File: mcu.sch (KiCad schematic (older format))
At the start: 6 parts

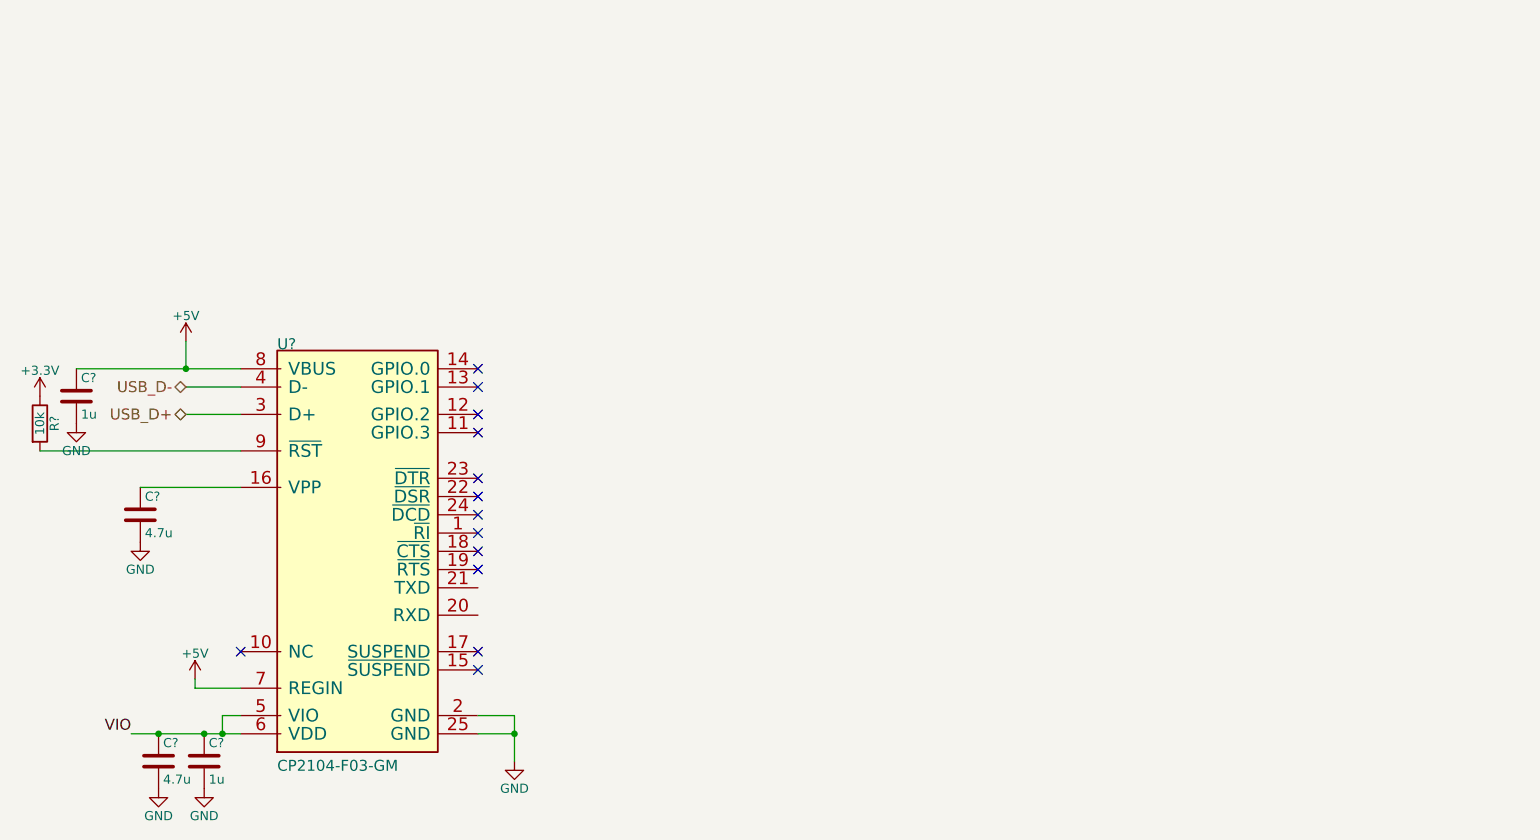
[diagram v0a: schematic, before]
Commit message: Finish basic MCU + USB/UART bridge schematics.
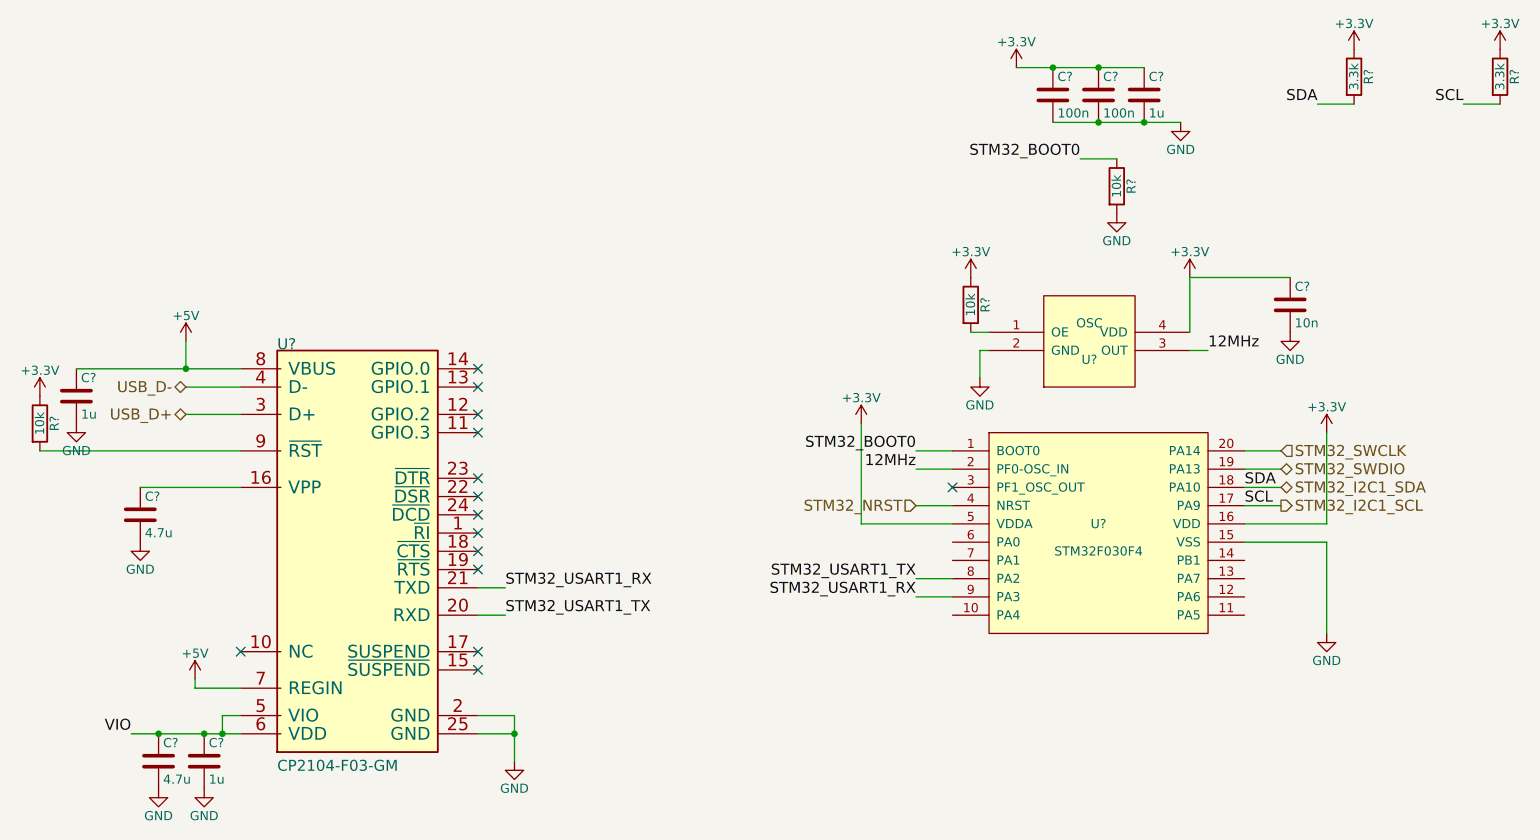
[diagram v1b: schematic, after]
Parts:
- added C?: 10n, symbol C
- added C? (x2): 100n, symbol C
- added C?: 1u, symbol C
- added R? (x2): 10k, symbol R
- added R? (x2): 3.3k, symbol R
- added U?: STM32F030F4, symbol STM32F030F4
- added U?: OSC, MODULE, symbol OSC
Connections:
- net +3V3: now also C?.1, C?.1, C?.1, C?.1, R?.1, R?.1, R?.1, U?.16 (VDD), U?.4 (VDD), U?.5 (VDDA)
- net GND: now also C?.2, C?.2, C?.2, C?.2, R?.2, U?.15 (VSS), U?.2 (GND)
- net STM32_USART1_TX: now reaches U?.20 (RXD)
- net STM32_USART1_TX: now also U?.8 (PA2)
- net STM32_USART1_RX: now reaches U?.21 (TXD)
- net STM32_USART1_RX: now also U?.9 (PA3)
- new net: R?.2, U?.1 (OE)
- new net 12MHz: U?.2 (PF0-OSC_IN), U?.3 (OUT)
- new net STM32_BOOT0: R?.1, U?.1 (BOOT0)
- new net STM32_I2C1_SCL: R?.2, U?.17 (PA9)
- new net STM32_I2C1_SDA: R?.2, U?.18 (PA10)
- new net STM32_NRST: U?.4 (NRST)
- new net STM32_SWCLK: U?.20 (PA14)
- new net STM32_SWDIO: U?.19 (PA13)
- no-connect marks 13 -> 14

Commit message: Add the config resistor dividers to the LTC3883 and output connectors, and a handful of test points. Schematic probably almost done at this point.
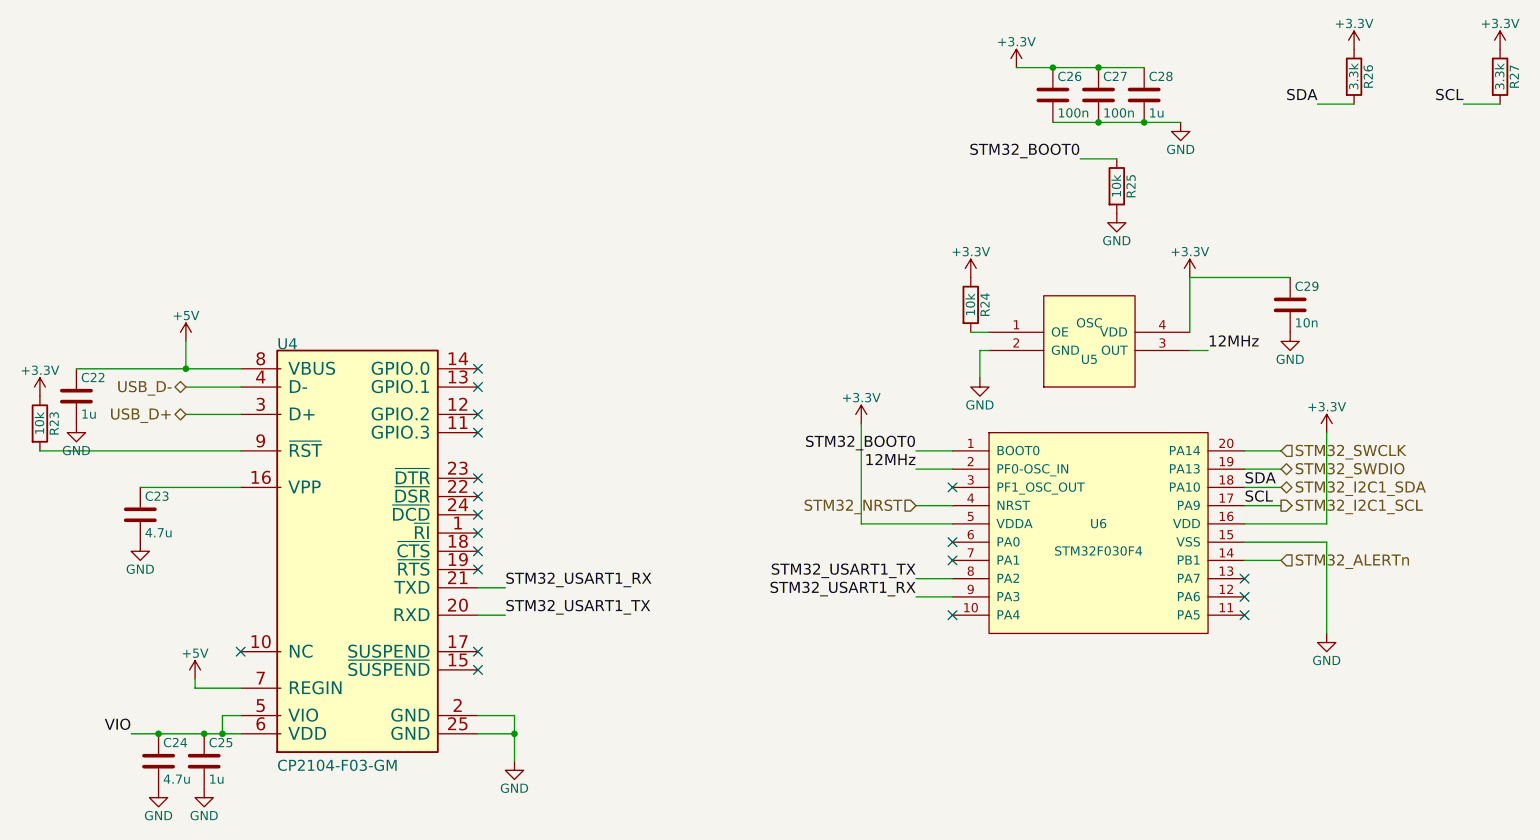
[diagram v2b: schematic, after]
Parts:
- gave numbers to parts that had none: 16
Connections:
- net STM32_ALERTn: now reaches U6.14 (PB1)
- no-connect marks 14 -> 20
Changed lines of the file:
@@
 $EndDescr
 $Comp
-L CP2104-F03-GM U?
+L CP2104-F03-GM U4
 U 1 1 569E6C41
 P 3550 2450
-F 0 "U?" H 3550 2450 60  0000 L BNN
+F 0 "U4" H 3550 2450 60  0000 L BNN
 F 1 "CP2104-F03-GM" H 3550 140 60  0000 L BNN
 F 2 "" H 3550 2450 60  0000 C CNN
@@
 $EndComp
 $Comp
-L +5V #PWR?
+L +5V #PWR41
 U 1 1 569E6CCC
 P 3050 2400
-F 0 "#PWR?" H 3050 2250 50  0001 C CNN
+F 0 "#PWR41" H 3050 2250 50  0001 C CNN
 F 1 "+5V" H 3050 2540 50  0000 C CNN
 F 2 "" H 3050 2400 50  0000 C CNN
@@
 $EndComp
 $Comp
-L C C?
+L C C22
 U 1 1 569E6CE5
 P 2450 2700
-F 0 "C?" H 2475 2800 50  0000 L CNN
+F 0 "C22" H 2475 2800 50  0000 L CNN
 F 1 "1u" H 2475 2600 50  0000 L CNN
 F 2 "" H 2488 2550 50  0000 C CNN
@@
 $EndComp
 $Comp
-L GND #PWR?
+L GND #PWR38
 U 1 1 569E6D2B
 P 2450 2850
-F 0 "#PWR?" H 2450 2600 50  0001 C CNN
+F 0 "#PWR38" H 2450 2600 50  0001 C CNN
 F 1 "GND" H 2450 2700 50  0000 C CNN
 F 2 "" H 2450 2850 50  0000 C CNN
@@
 $EndComp
 $Comp
-L C C?
+L C C23
 U 1 1 569E6D69
 P 2800 3350
-F 0 "C?" H 2825 3450 50  0000 L CNN
+F 0 "C23" H 2825 3450 50  0000 L CNN
 F 1 "4.7u" H 2825 3250 50  0000 L CNN
 F 2 "" H 2838 3200 50  0000 C CNN
@@
 $EndComp
 $Comp
-L GND #PWR?
+L GND #PWR39
 U 1 1 569E6DB5
 P 2800 3500
-F 0 "#PWR?" H 2800 3250 50  0001 C CNN
+F 0 "#PWR39" H 2800 3250 50  0001 C CNN
 F 1 "GND" H 2800 3350 50  0000 C CNN
 F 2 "" H 2800 3500 50  0000 C CNN
@@
 $EndComp
 $Comp
-L R R?
+L R R23
 U 1 1 569E6E19
 P 2250 2850
-F 0 "R?" V 2330 2850 50  0000 C CNN
+F 0 "R23" V 2330 2850 50  0000 C CNN
 F 1 "10k" V 2250 2850 50  0000 C CNN
 F 2 "" V 2180 2850 50  0000 C CNN
@@
 $EndComp
 $Comp
-L +5V #PWR?
+L +5V #PWR42
 U 1 1 569E6EA3
 P 3100 4250
-F 0 "#PWR?" H 3100 4100 50  0001 C CNN
+F 0 "#PWR42" H 3100 4100 50  0001 C CNN
 F 1 "+5V" H 3100 4390 50  0000 C CNN
 F 2 "" H 3100 4250 50  0000 C CNN
@@
 NoConn ~ 3350 4100
 $Comp
-L GND #PWR?
+L GND #PWR44
 U 1 1 569E6ED3
 P 4850 4700
-F 0 "#PWR?" H 4850 4450 50  0001 C CNN
+F 0 "#PWR44" H 4850 4450 50  0001 C CNN
 F 1 "GND" H 4850 4550 50  0000 C CNN
 F 2 "" H 4850 4700 50  0000 C CNN
@@
 NoConn ~ 4650 2550
 $Comp
-L C C?
+L C C25
 U 1 1 569E7001
 P 3150 4700
-F 0 "C?" H 3175 4800 50  0000 L CNN
+F 0 "C25" H 3175 4800 50  0000 L CNN
 F 1 "1u" H 3175 4600 50  0000 L CNN
 F 2 "" H 3188 4550 50  0000 C CNN
@@
 $EndComp
 $Comp
-L C C?
+L C C24
 U 1 1 569E7040
 P 2900 4700
-F 0 "C?" H 2925 4800 50  0000 L CNN
+F 0 "C24" H 2925 4800 50  0000 L CNN
 F 1 "4.7u" H 2925 4600 50  0000 L CNN
 F 2 "" H 2938 4550 50  0000 C CNN
@@
 $EndComp
 $Comp
-L GND #PWR?
+L GND #PWR40
 U 1 1 569E70FE
 P 2900 4850
-F 0 "#PWR?" H 2900 4600 50  0001 C CNN
+F 0 "#PWR40" H 2900 4600 50  0001 C CNN
 F 1 "GND" H 2900 4700 50  0000 C CNN
 F 2 "" H 2900 4850 50  0000 C CNN
@@
 $EndComp
 $Comp
-L GND #PWR?
+L GND #PWR43
 U 1 1 569E7122
 P 3150 4850
-F 0 "#PWR?" H 3150 4600 50  0001 C CNN
+F 0 "#PWR43" H 3150 4600 50  0001 C CNN
 F 1 "GND" H 3150 4700 50  0000 C CNN
 F 2 "" H 3150 4850 50  0000 C CNN
@@
 VIO
 $Comp
-L +3.3V #PWR?
+L +3.3V #PWR37
 U 1 1 569E73C1
 P 2250 2700
-F 0 "#PWR?" H 2250 2550 50  0001 C CNN
+F 0 "#PWR37" H 2250 2550 50  0001 C CNN
 F 1 "+3.3V" H 2250 2840 50  0000 C CNN
 F 2 "" H 2250 2700 50  0000 C CNN
@@
 $EndComp
 $Comp
-L STM32F030F4 U?
+L STM32F030F4 U6
 U 1 1 569E8A8D
 P 8050 3450
-F 0 "U?" H 8050 3500 50  0000 C CNN
+F 0 "U6" H 8050 3500 50  0000 C CNN
 F 1 "STM32F030F4" H 8050 3350 50  0000 C CNN
 F 2 "" H 8050 3450 60  0000 C CNN
@@
 NoConn ~ 7250 3200
 $Comp
-L OSC U?
+L OSC U5
 U 1 1 569E8BDE
 P 8000 2400
-F 0 "U?" H 8000 2300 50  0000 C CNN
+F 0 "U5" H 8000 2300 50  0000 C CNN
 F 1 "OSC" H 8000 2500 50  0000 C CNN
 F 2 "MODULE" H 8000 2200 50  0001 C CNN
@@
 $EndComp
 $Comp
-L R R?
+L R R24
 U 1 1 569E911B
 P 7350 2200
-F 0 "R?" V 7430 2200 50  0000 C CNN
+F 0 "R24" V 7430 2200 50  0000 C CNN
 F 1 "10k" V 7350 2200 50  0000 C CNN
 F 2 "" V 7280 2200 50  0000 C CNN
@@
 $EndComp
 $Comp
-L +3.3V #PWR?
+L +3.3V #PWR46
 U 1 1 569E917D
 P 7350 2050
-F 0 "#PWR?" H 7350 1900 50  0001 C CNN
+F 0 "#PWR46" H 7350 1900 50  0001 C CNN
 F 1 "+3.3V" H 7350 2190 50  0000 C CNN
 F 2 "" H 7350 2050 50  0000 C CNN
@@
 $EndComp
 $Comp
-L +3.3V #PWR?
+L +3.3V #PWR51
 U 1 1 569E91AA
 P 8550 2050
-F 0 "#PWR?" H 8550 1900 50  0001 C CNN
+F 0 "#PWR51" H 8550 1900 50  0001 C CNN
 F 1 "+3.3V" H 8550 2190 50  0000 C CNN
 F 2 "" H 8550 2050 50  0000 C CNN
@@
 $EndComp
 $Comp
-L C C?
+L C C29
 U 1 1 569E91E8
 P 9100 2200
-F 0 "C?" H 9125 2300 50  0000 L CNN
+F 0 "C29" H 9125 2300 50  0000 L CNN
 F 1 "10n" H 9125 2100 50  0000 L CNN
 F 2 "" H 9138 2050 50  0000 C CNN
@@
 $EndComp
 $Comp
-L GND #PWR?
+L GND #PWR52
 U 1 1 569E9259
 P 9100 2350
-F 0 "#PWR?" H 9100 2100 50  0001 C CNN
+F 0 "#PWR52" H 9100 2100 50  0001 C CNN
 F 1 "GND" H 9100 2200 50  0000 C CNN
 F 2 "" H 9100 2350 50  0000 C CNN
@@
 $EndComp
 $Comp
-L GND #PWR?
+L GND #PWR47
 U 1 1 569E92B9
 P 7400 2600
-F 0 "#PWR?" H 7400 2350 50  0001 C CNN
+F 0 "#PWR47" H 7400 2350 50  0001 C CNN
 F 1 "GND" H 7400 2450 50  0000 C CNN
 F 2 "" H 7400 2600 50  0000 C CNN
@@
 STM32_BOOT0
 $Comp
-L R R?
+L R R25
 U 1 1 569E94C2
 P 8150 1550
-F 0 "R?" V 8230 1550 50  0000 C CNN
+F 0 "R25" V 8230 1550 50  0000 C CNN
 F 1 "10k" V 8150 1550 50  0000 C CNN
 F 2 "" V 8080 1550 50  0000 C CNN
@@
 $EndComp
 $Comp
-L GND #PWR?
+L GND #PWR49
 U 1 1 569E953A
 P 8150 1700
-F 0 "#PWR?" H 8150 1450 50  0001 C CNN
+F 0 "#PWR49" H 8150 1450 50  0001 C CNN
 F 1 "GND" H 8150 1550 50  0000 C CNN
 F 2 "" H 8150 1700 50  0000 C CNN
@@
 SCL
 $Comp
-L +3.3V #PWR?
+L +3.3V #PWR53
 U 1 1 569E9CE2
 P 9300 2900
-F 0 "#PWR?" H 9300 2750 50  0001 C CNN
+F 0 "#PWR53" H 9300 2750 50  0001 C CNN
 F 1 "+3.3V" H 9300 3040 50  0000 C CNN
 F 2 "" H 9300 2900 50  0000 C CNN
@@
 $EndComp
 $Comp
-L GND #PWR?
+L GND #PWR54
 U 1 1 569E9DAE
 P 9300 4000
-F 0 "#PWR?" H 9300 3750 50  0001 C CNN
+F 0 "#PWR54" H 9300 3750 50  0001 C CNN
 F 1 "GND" H 9300 3850 50  0000 C CNN
 F 2 "" H 9300 4000 50  0000 C CNN
@@
 $EndComp
 $Comp
-L +3.3V #PWR?
+L +3.3V #PWR48
 U 1 1 569E9E93
 P 7600 900
-F 0 "#PWR?" H 7600 750 50  0001 C CNN
+F 0 "#PWR48" H 7600 750 50  0001 C CNN
 F 1 "+3.3V" H 7600 1040 50  0000 C CNN
 F 2 "" H 7600 900 50  0000 C CNN
@@
 $EndComp
 $Comp
-L C C?
+L C C26
 U 1 1 569E9FA8
 P 7800 1050
-F 0 "C?" H 7825 1150 50  0000 L CNN
+F 0 "C26" H 7825 1150 50  0000 L CNN
 F 1 "100n" H 7825 950 50  0000 L CNN
 F 2 "" H 7838 900 50  0000 C CNN
@@
 $EndComp
 $Comp
-L C C?
+L C C27
 U 1 1 569E9FE5
 P 8050 1050
-F 0 "C?" H 8075 1150 50  0000 L CNN
+F 0 "C27" H 8075 1150 50  0000 L CNN
 F 1 "100n" H 8075 950 50  0000 L CNN
 F 2 "" H 8088 900 50  0000 C CNN
@@
 $EndComp
 $Comp
-L C C?
+L C C28
 U 1 1 569EA02A
 P 8300 1050
-F 0 "C?" H 8325 1150 50  0000 L CNN
+F 0 "C28" H 8325 1150 50  0000 L CNN
 F 1 "1u" H 8325 950 50  0000 L CNN
 F 2 "" H 8338 900 50  0000 C CNN
@@
 $EndComp
 $Comp
-L GND #PWR?
+L GND #PWR50
 U 1 1 569EA23E
 P 8500 1200
-F 0 "#PWR?" H 8500 950 50  0001 C CNN
+F 0 "#PWR50" H 8500 950 50  0001 C CNN
 F 1 "GND" H 8500 1050 50  0000 C CNN
 F 2 "" H 8500 1200 50  0000 C CNN
@@
 SDA
 $Comp
-L R R?
+L R R26
 U 1 1 569EA6B7
 P 9450 950
-F 0 "R?" V 9530 950 50  0000 C CNN
+F 0 "R26" V 9530 950 50  0000 C CNN
 F 1 "3.3k" V 9450 950 50  0000 C CNN
 F 2 "" V 9380 950 50  0000 C CNN
@@
 $EndComp
 $Comp
-L +3.3V #PWR?
+L +3.3V #PWR55
 U 1 1 569EA769
 P 9450 800
-F 0 "#PWR?" H 9450 650 50  0001 C CNN
+F 0 "#PWR55" H 9450 650 50  0001 C CNN
 F 1 "+3.3V" H 9450 940 50  0000 C CNN
 F 2 "" H 9450 800 50  0000 C CNN
@@
 SCL
 $Comp
-L R R?
+L R R27
 U 1 1 569EA896
 P 10250 950
-F 0 "R?" V 10330 950 50  0000 C CNN
+F 0 "R27" V 10330 950 50  0000 C CNN
 F 1 "3.3k" V 10250 950 50  0000 C CNN
 F 2 "" V 10180 950 50  0000 C CNN
@@
 $EndComp
 $Comp
-L +3.3V #PWR?
+L +3.3V #PWR56
 U 1 1 569EA89C
 P 10250 800
-F 0 "#PWR?" H 10250 650 50  0001 C CNN
+F 0 "#PWR56" H 10250 650 50  0001 C CNN
 F 1 "+3.3V" H 10250 940 50  0000 C CNN
 F 2 "" H 10250 800 50  0000 C CNN
@@
 	10050 1100 10250 1100
 $Comp
-L +3.3V #PWR?
+L +3.3V #PWR45
 U 1 1 569EAA8C
 P 6750 2850
-F 0 "#PWR?" H 6750 2700 50  0001 C CNN
+F 0 "#PWR45" H 6750 2700 50  0001 C CNN
 F 1 "+3.3V" H 6750 2990 50  0000 C CNN
 F 2 "" H 6750 2850 50  0000 C CNN
@@
 Wire Wire Line
 	6750 3400 7250 3400
+Text HLabel 9050 3600 2    60   Input ~ 0
+STM32_ALERTn
+Wire Wire Line
+	9050 3600 8850 3600
+NoConn ~ 8850 3700
+NoConn ~ 8850 3800
+NoConn ~ 8850 3900
+NoConn ~ 7250 3900
+NoConn ~ 7250 3600
+NoConn ~ 7250 3500
 $EndSCHEMATC
